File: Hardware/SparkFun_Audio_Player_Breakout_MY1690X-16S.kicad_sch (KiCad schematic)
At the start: 41 parts, among them J1 3.5mm TRRS, J2 Conn_01x03, J3 Conn_01x02, J4 USB_C_Receptacle, J5 Conn_01x06, J6 microSD, Q1 BSS138, U2 MY1690X-16S

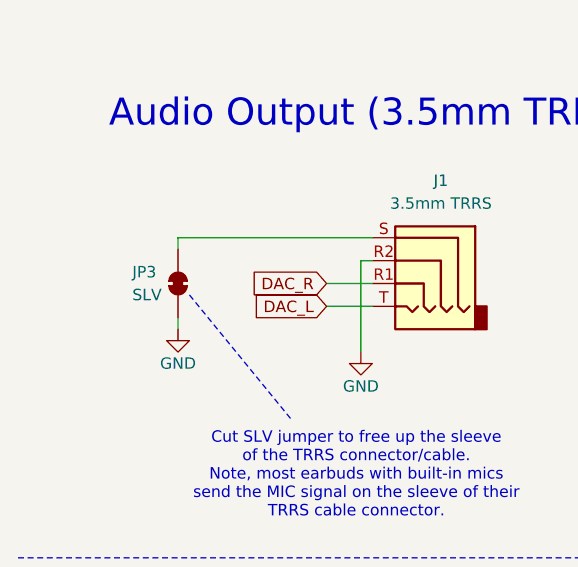
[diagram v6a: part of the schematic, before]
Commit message: repositioned connectors to have over-hang
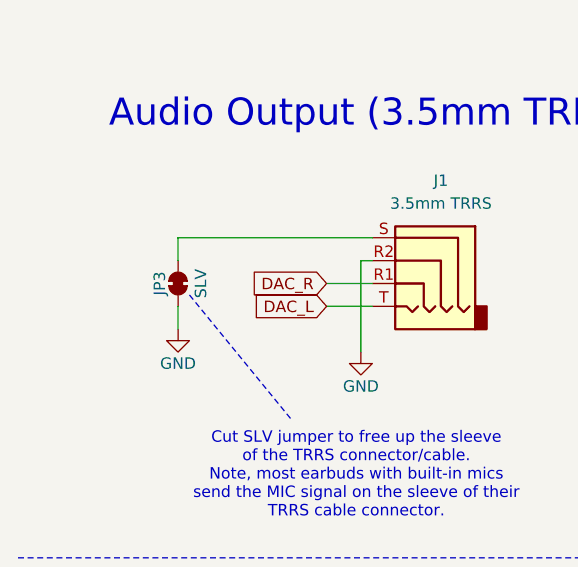
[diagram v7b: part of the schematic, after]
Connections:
- net GND: now also JP3.1 (A); no longer JP3.2 (B)
- net at J1.S: now also JP3.2 (B); no longer JP3.1 (A)
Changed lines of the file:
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@@
 	(wire
 		(pts
-			(xy 30.48 118.11) (xy 30.48 119.38)
-		)
-		(stroke
-			(width 0)
-			(type default)
-		)
-	)
-	(wire
-		(pts
 			(xy 210.82 139.7) (xy 210.82 142.24)
 		)
@@
 	(wire
 		(pts
-			(xy 30.48 109.22) (xy 30.48 110.49)
-		)
-		(stroke
-			(width 0)
-			(type default)
-		)
-	)
-	(wire
-		(pts
 			(xy 231.14 50.8) (xy 232.41 50.8)
 		)
@@
 	(wire
 		(pts
+			(xy 30.48 109.22) (xy 30.48 111.76)
+		)
+		(stroke
+			(width 0)
+			(type default)
+		)
+	)
+	(wire
+		(pts
 			(xy 255.27 57.15) (xy 255.27 55.88)
 		)
@@
 		)
 	)
+	(wire
+		(pts
+			(xy 30.48 116.84) (xy 30.48 119.38)
+		)
+		(stroke
+			(width 0)
+			(type default)
+		)
+	)
 	(polyline
 		(pts
@@
 	)
 	(symbol
-		(lib_name "SolderJumper_2_Bridged_1")
-		(lib_id "SparkFun-Jumper:SolderJumper_2_Bridged")
-		(at 30.48 114.3 270)
-		(unit 1)
-		(exclude_from_sim no)
-		(in_bom yes)
-		(on_board yes)
-		(dnp no)
-		(property "Reference" "JP3"
-			(at 25.4 113.03 90)
-			(effects
-				(font
-					(size 1.27 1.27)
-				)
-				(justify left)
-			)
-		)
-		(property "Value" "SLV"
-			(at 25.4 115.57 90)
-			(effects
-				(font
-					(size 1.27 1.27)
-				)
-				(justify left)
-			)
-		)
-		(property "Footprint" "SparkFun-Jumper:Jumper_2_NC_Trace"
-			(at 25.908 114.046 0)
-			(effects
-				(font
-					(size 1.27 1.27)
-				)
-				(hide yes)
-			)
-		)
-		(property "Datasheet" "~"
-			(at 22.86 114.3 0)
-			(effects
-				(font
-					(size 1.27 1.27)
-				)
-				(hide yes)
-			)
-		)
-		(property "Description" "Solder Jumper, 2-pole, closed/bridged"
-			(at 20.32 114.3 0)
-			(effects
-				(font
-					(size 1.27 1.27)
-				)
-				(hide yes)
-			)
-		)
-		(pin "1"
-		)
-		(pin "2"
-		)
-		(instances
-			(project ""
-				(path "/e3dd3ae4-244d-4cba-9cca-5d2abf83f29a"
-					(reference "JP3")
-					(unit 1)
-				)
-			)
-		)
-	)
-	(symbol
 		(lib_id "SparkFun-DiscreteSemi:D_Schottky_3A_10V_0.28V")
 		(at 45.72 171.45 270)
@@
 					(unit 1)
 				)
+			)
+		)
+	)
+	(symbol
+		(lib_id "SparkFun-Jumper:SolderJumper_2_Bridged")
+		(at 30.48 114.3 90)
+		(unit 1)
+		(exclude_from_sim no)
+		(in_bom yes)
+		(on_board yes)
+		(dnp no)
+		(fields_autoplaced yes)
+		(property "Reference" "JP3"
+			(at 28.448 114.3 0)
+			(effects
+				(font
+					(size 1.27 1.27)
+				)
+			)
+		)
+		(property "Value" "SLV"
+			(at 33.02 114.3 0)
+			(effects
+				(font
+					(size 1.27 1.27)
+				)
+			)
+		)
+		(property "Footprint" "SparkFun-Jumper:Jumper_2_NC_Trace"
+			(at 35.052 114.554 0)
+			(effects
+				(font
+					(size 1.27 1.27)
+				)
+				(hide yes)
+			)
+		)
+		(property "Datasheet" "~"
+			(at 38.1 114.3 0)
+			(effects
+				(font
+					(size 1.27 1.27)
+				)
+				(hide yes)
+			)
+		)
+		(property "Description" "Solder Jumper, 2-pole, closed/bridged"
+			(at 30.48 114.3 0)
+			(effects
+				(font
+					(size 1.27 1.27)
+				)
+				(hide yes)
+			)
+		)
+		(pin "1"
+		)
+		(pin "2"
+		)
+		(instances
+			(project "SparkFun_Audio_Player_Breakout_MY1690X-16S"
+				(path "/e3dd3ae4-244d-4cba-9cca-5d2abf83f29a"
+					(reference "JP3")
+					(unit 1)
+				)

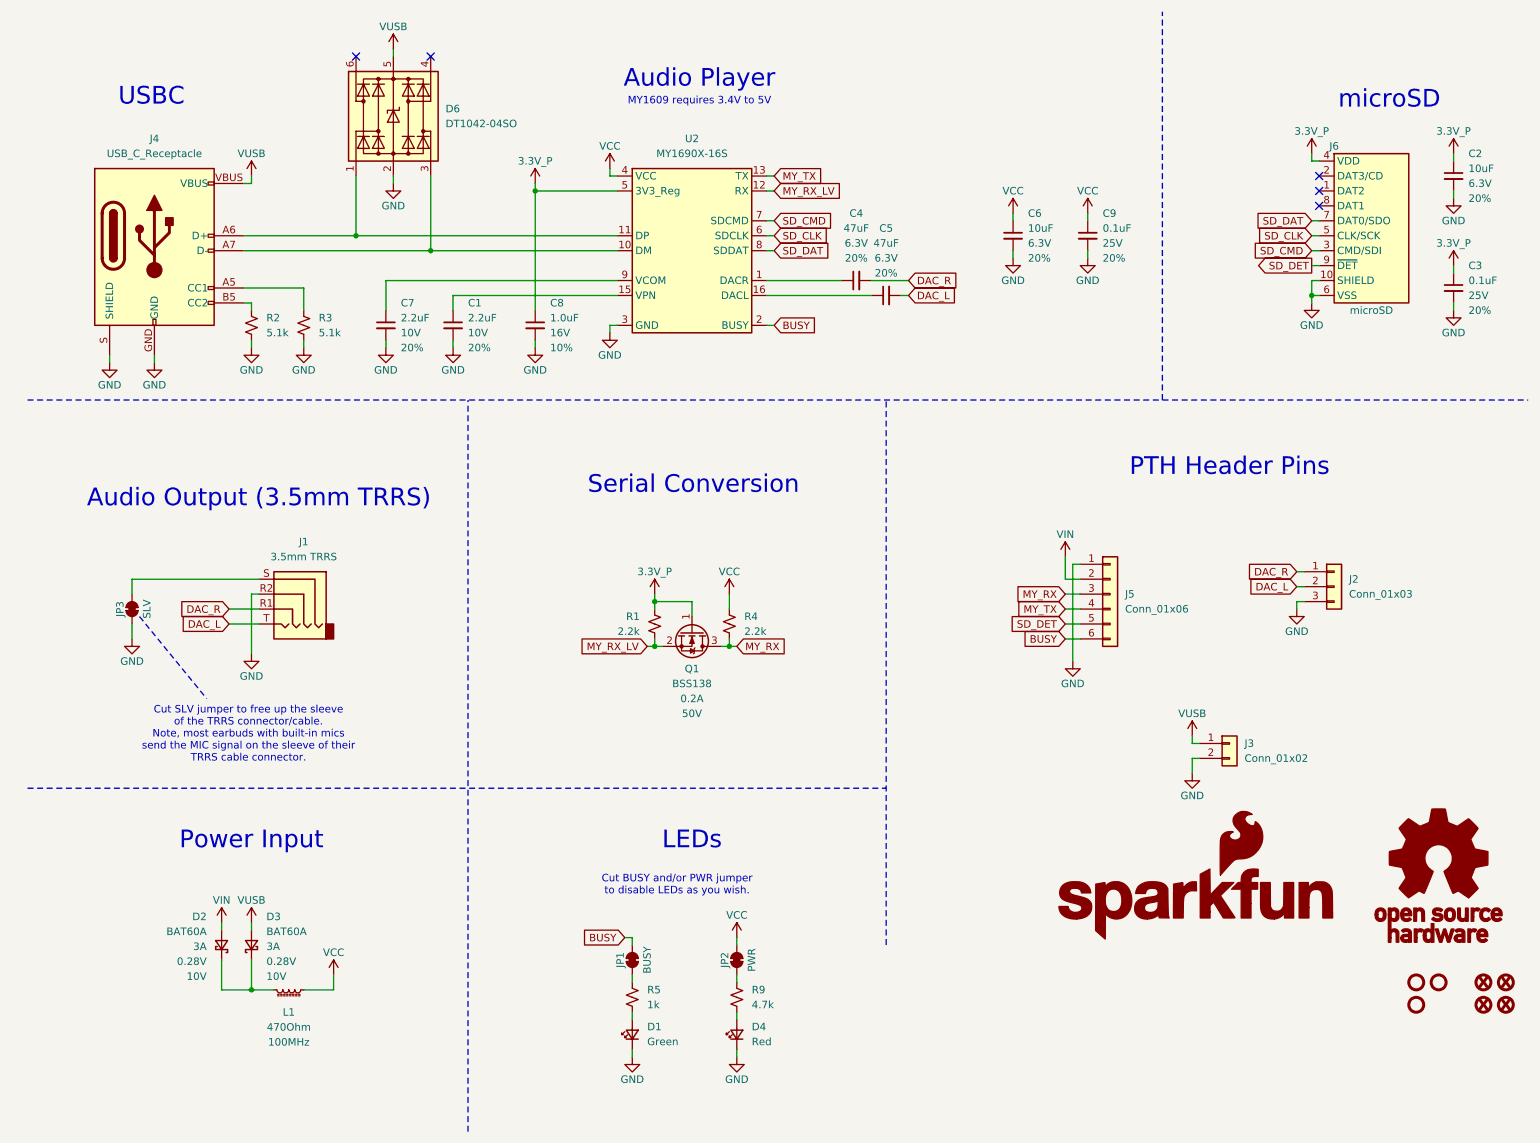
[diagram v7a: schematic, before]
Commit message: checklist eng run
-added ordering instruction about NPTH holes (under the TRRS connector)
-sch cleanup
-add VIN range in SCH and BRD
-add "1234" text objects to each layer
-nudges a via under LOUT silk
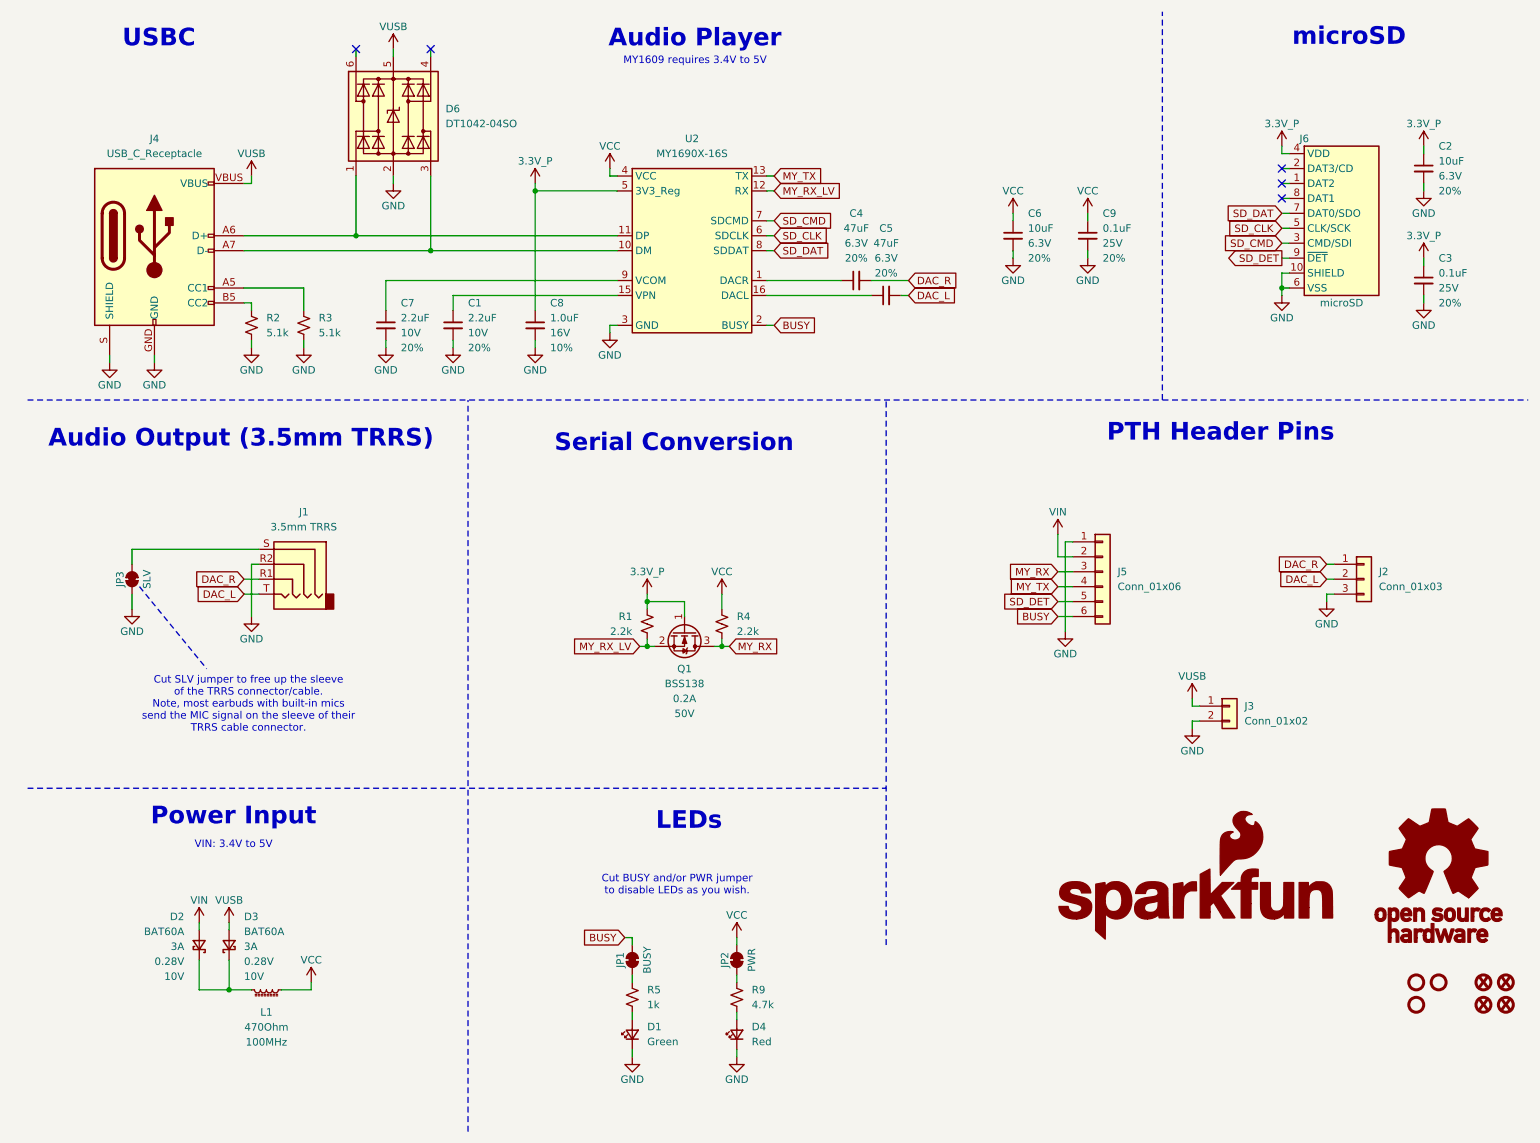
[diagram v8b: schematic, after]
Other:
- note added: "VIN: 3.4V to 5V"
- moved on the sheet: C2, C3, D2, D3, J1, J2, J3, J5, J6, JP3, L1, Q1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
